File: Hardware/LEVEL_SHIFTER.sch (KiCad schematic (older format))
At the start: 3 parts

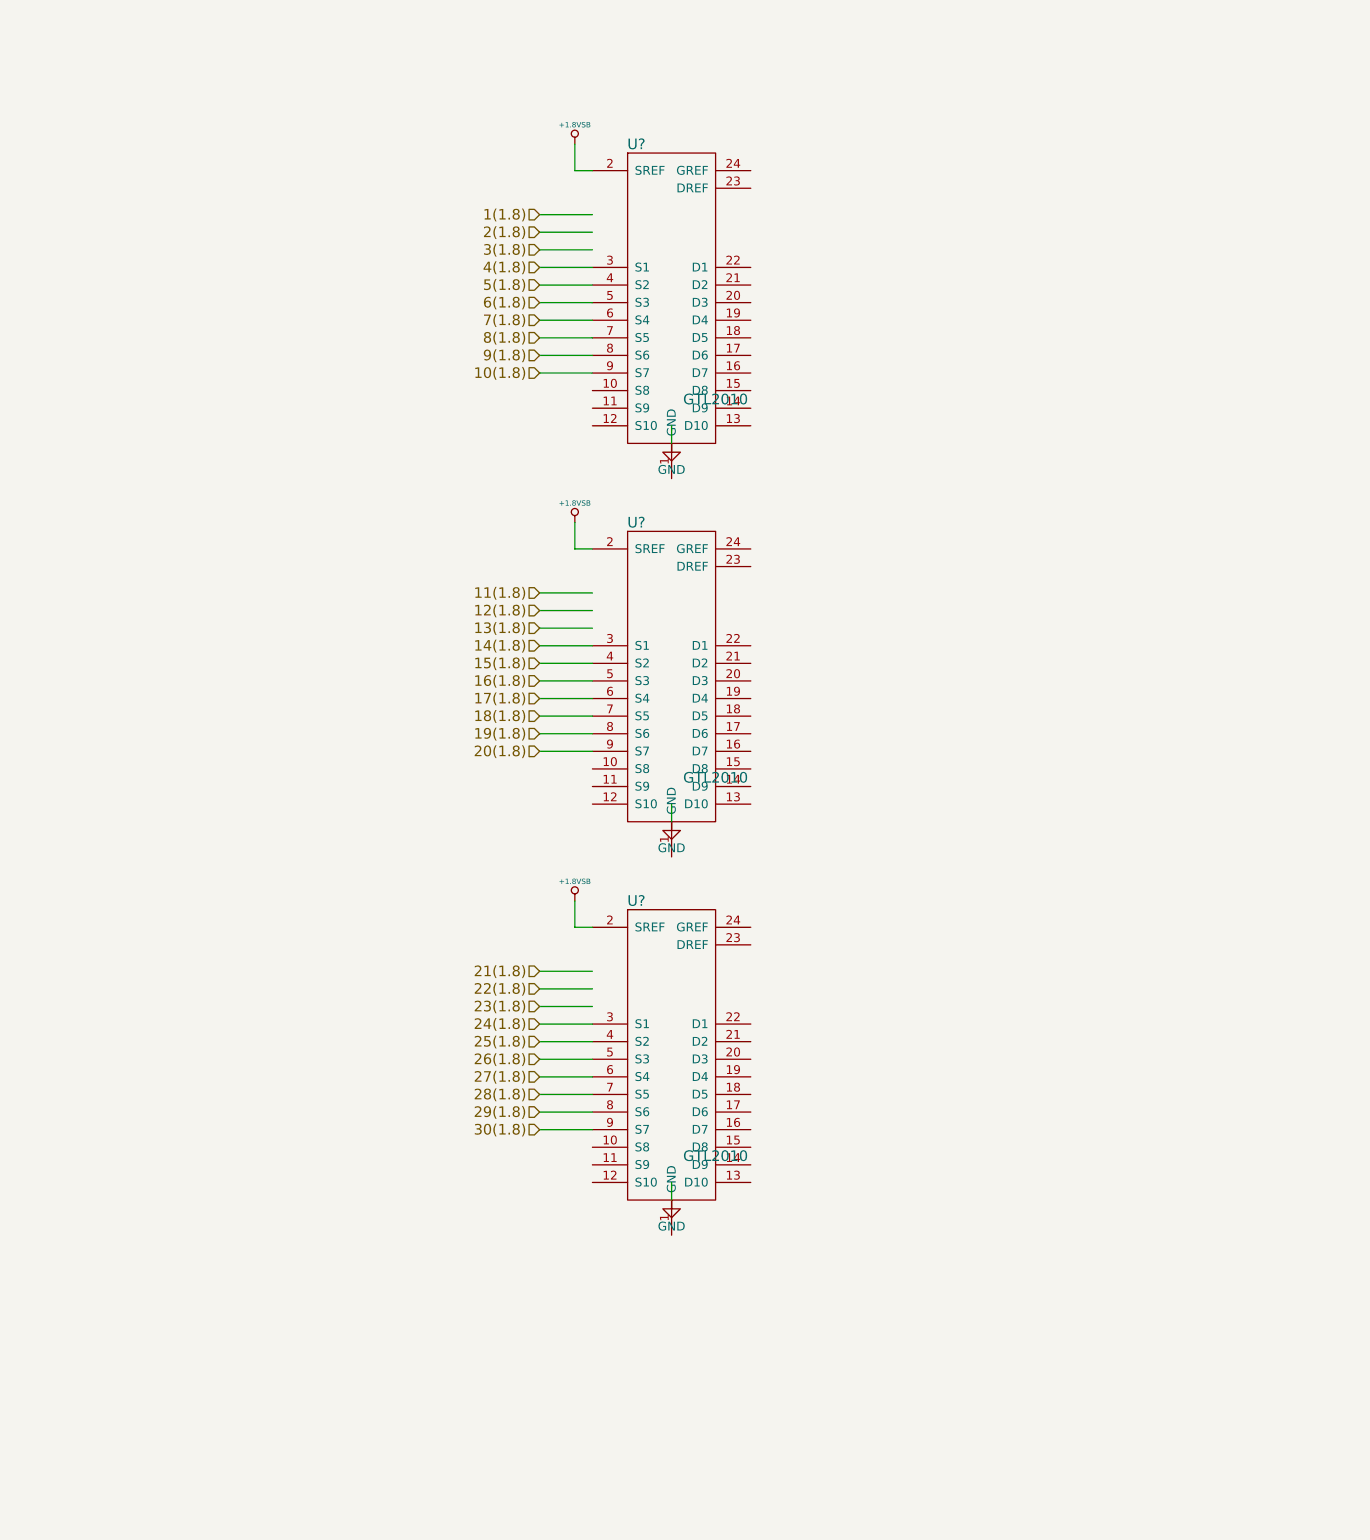
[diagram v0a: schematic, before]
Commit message: Currently adding level shifters
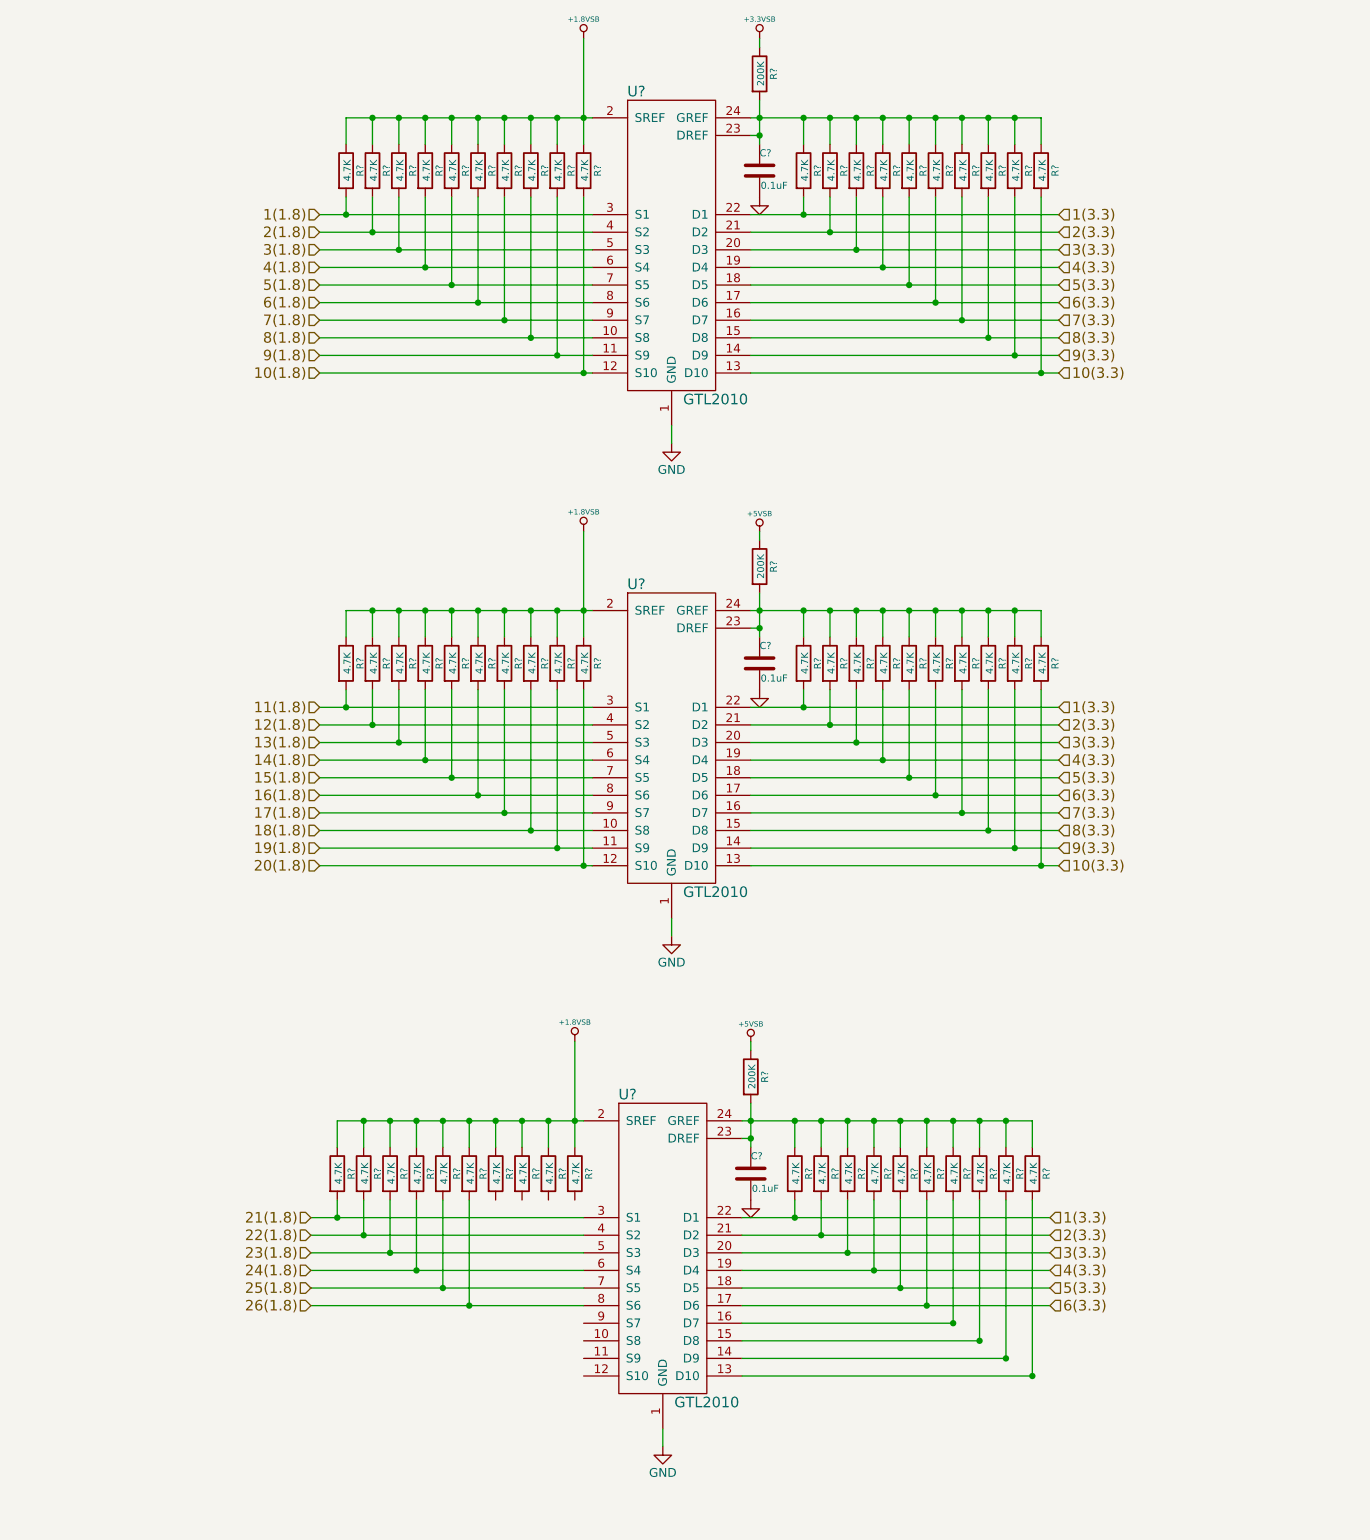
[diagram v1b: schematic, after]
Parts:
- removed U? (x2): GTL2010, symbol GTL2010
- added C? (x3): 0.1uF, symbol C-RESCUE-museV2
- added R? (x60): 4.7K, symbol R-RESCUE-museV2
- added R? (x3): 200K, symbol R-RESCUE-museV2
- added U? (x2): GTL2010, symbol GTL2010
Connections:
- net labels added: +3.3VSB, +5VSB, 1(3.3), 10(3.3), 2(3.3), 3(3.3), 4(3.3), 5(3.3), 6(3.3), 7(3.3), 8(3.3), 9(3.3)
- net labels removed: 27(1.8), 28(1.8), 29(1.8), 30(1.8)
- wire segments 39 -> 308
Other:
- moved on the sheet: U?

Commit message: Finished level shifter sheet
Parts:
- removed R? (x8): 4.7K, symbol R-RESCUE-museV2
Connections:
- net 1(3.3): no longer R?.2, R?.2, U?.22 (D1), U?.22 (D1)
- net 10(3.3): no longer R?.2, U?.13 (D10)
- net 2(3.3): no longer R?.2, R?.2, U?.21 (D2), U?.21 (D2)
- net 3(3.3): no longer R?.2, R?.2, U?.20 (D3), U?.20 (D3)
- net 4(3.3): no longer R?.2, R?.2, U?.19 (D4), U?.19 (D4)
- net 5(3.3): no longer R?.2, R?.2, U?.18 (D5), U?.18 (D5)
- net 6(3.3): no longer R?.2, R?.2, U?.17 (D6), U?.17 (D6)
- net 7(3.3): no longer R?.2, U?.16 (D7)
- net 8(3.3): no longer R?.2, U?.15 (D8)
- net 9(3.3): no longer R?.2, U?.14 (D9)
- new net 1(5.0): R?.2, U?.22 (D1)
- new net 10(5.0): R?.2, U?.13 (D10)
- new net 11(5.0): R?.2, U?.22 (D1)
- new net 12(5.0): R?.2, U?.21 (D2)
- new net 13(5.0): R?.2, U?.20 (D3)
- new net 14(5.0): R?.2, U?.19 (D4)
- new net 15(5.0): R?.2, U?.18 (D5)
- new net 16(5.0): R?.2, U?.17 (D6)
- new net 2(5.0): R?.2, U?.21 (D2)
- new net 3(5.0): R?.2, U?.20 (D3)
- new net 4(5.0): R?.2, U?.19 (D4)
- new net 5(5.0): R?.2, U?.18 (D5)
- new net 6(5.0): R?.2, U?.17 (D6)
- new net 7(5.0): R?.2, U?.16 (D7)
- new net 8(5.0): R?.2, U?.15 (D8)
- new net 9(5.0): R?.2, U?.14 (D9)
- no-connect marks 0 -> 8
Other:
- moved on the sheet: C?, R?, U?

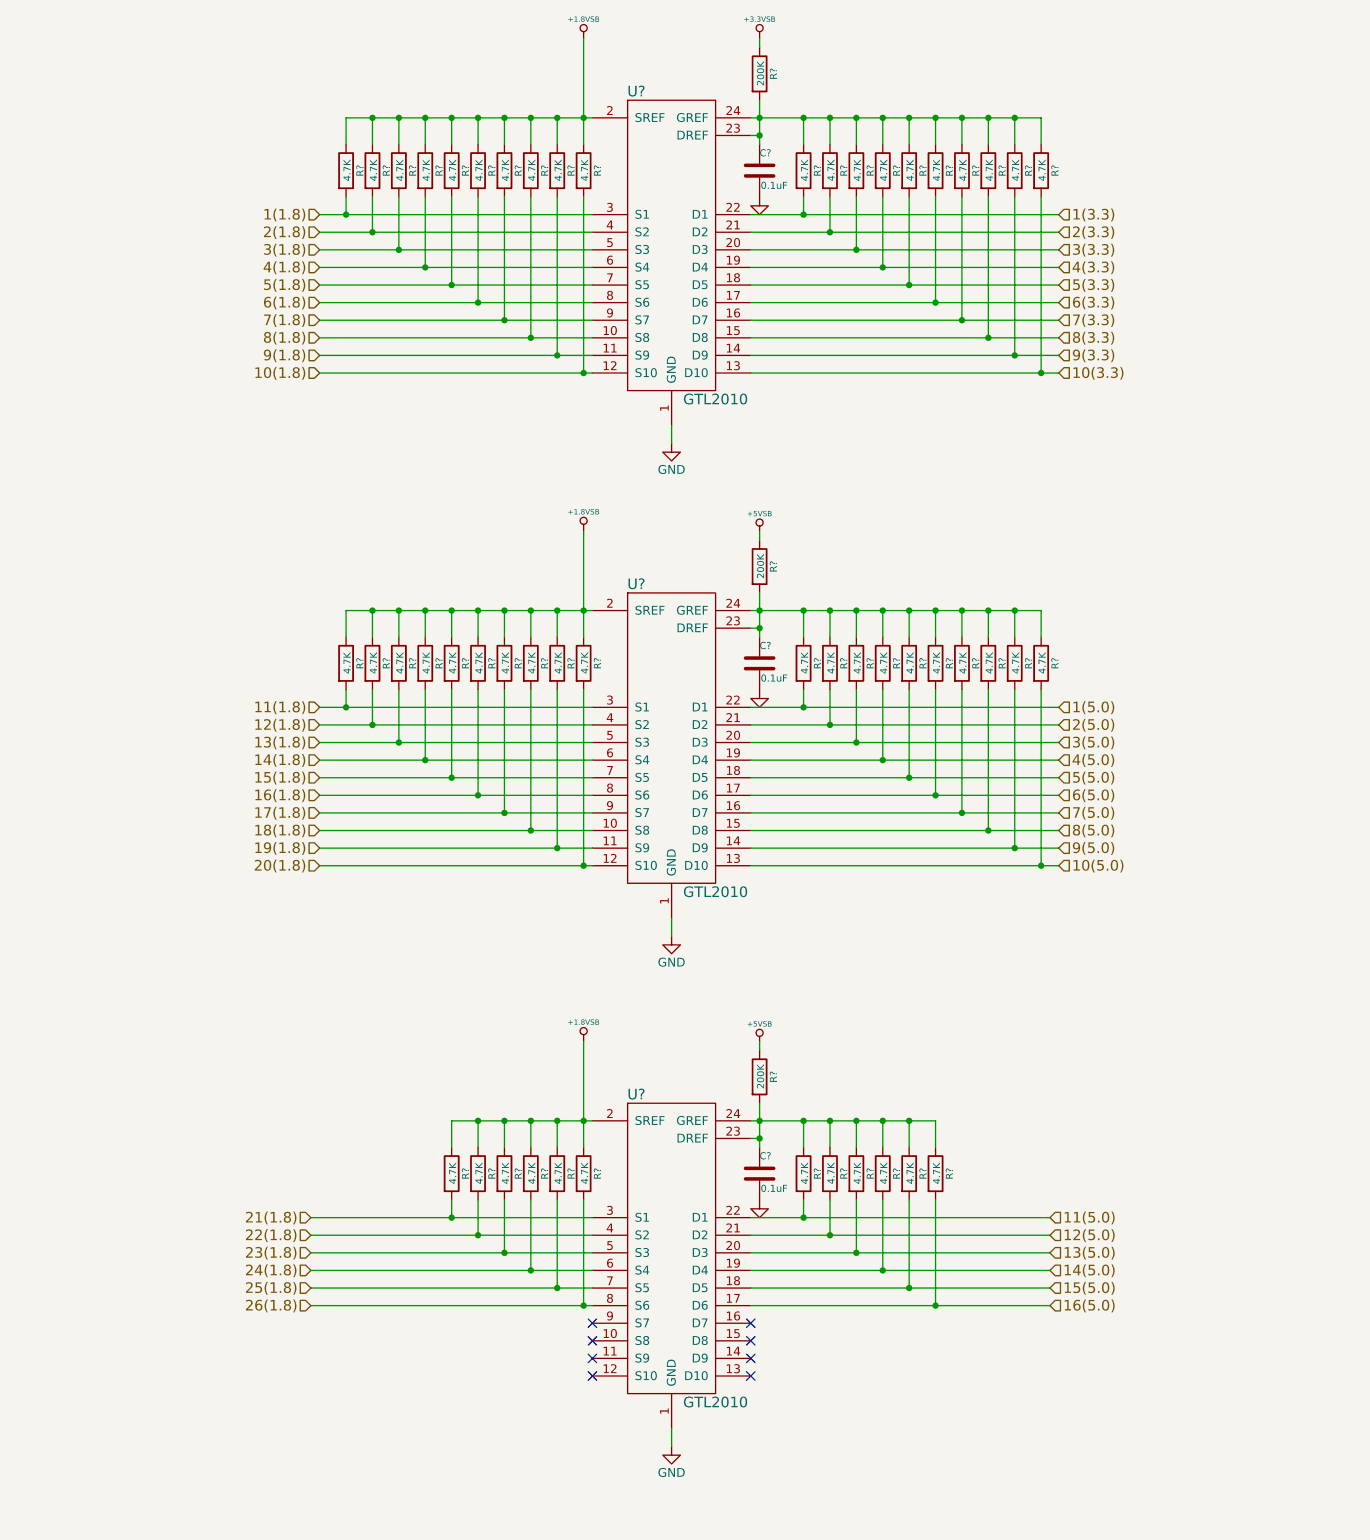
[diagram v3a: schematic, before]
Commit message: Changing to global labels/pages in progress
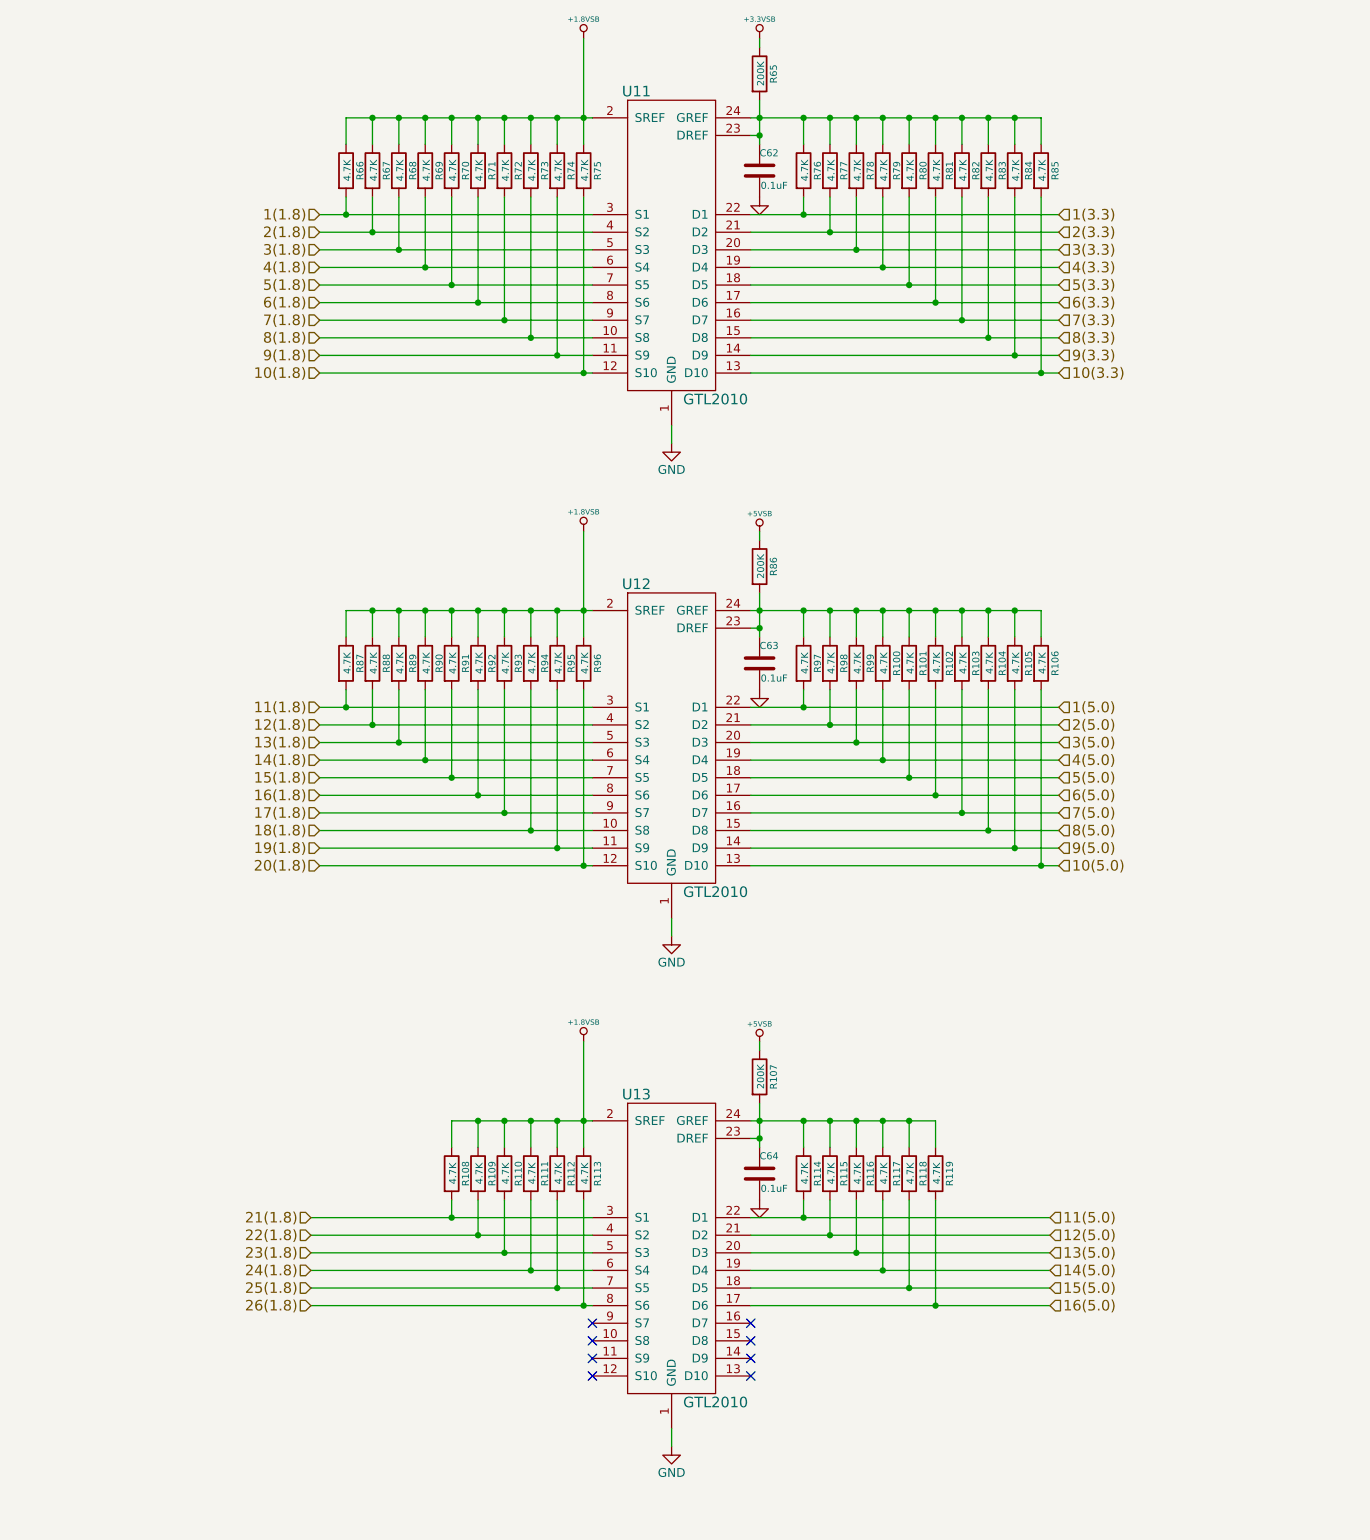
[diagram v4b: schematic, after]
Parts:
- gave numbers to parts that had none: 61
